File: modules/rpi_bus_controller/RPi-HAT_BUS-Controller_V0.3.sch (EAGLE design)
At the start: 66 parts, among them IC1 MC34063AD, IC2 ADUM1201ARZ, IC3 P89LPC922FDH,512FDH, IC4 24LC-I/OT, IC5 LPC1115, Q1 ASF1, T1 BC856, T2 BCP52, T3 BC847

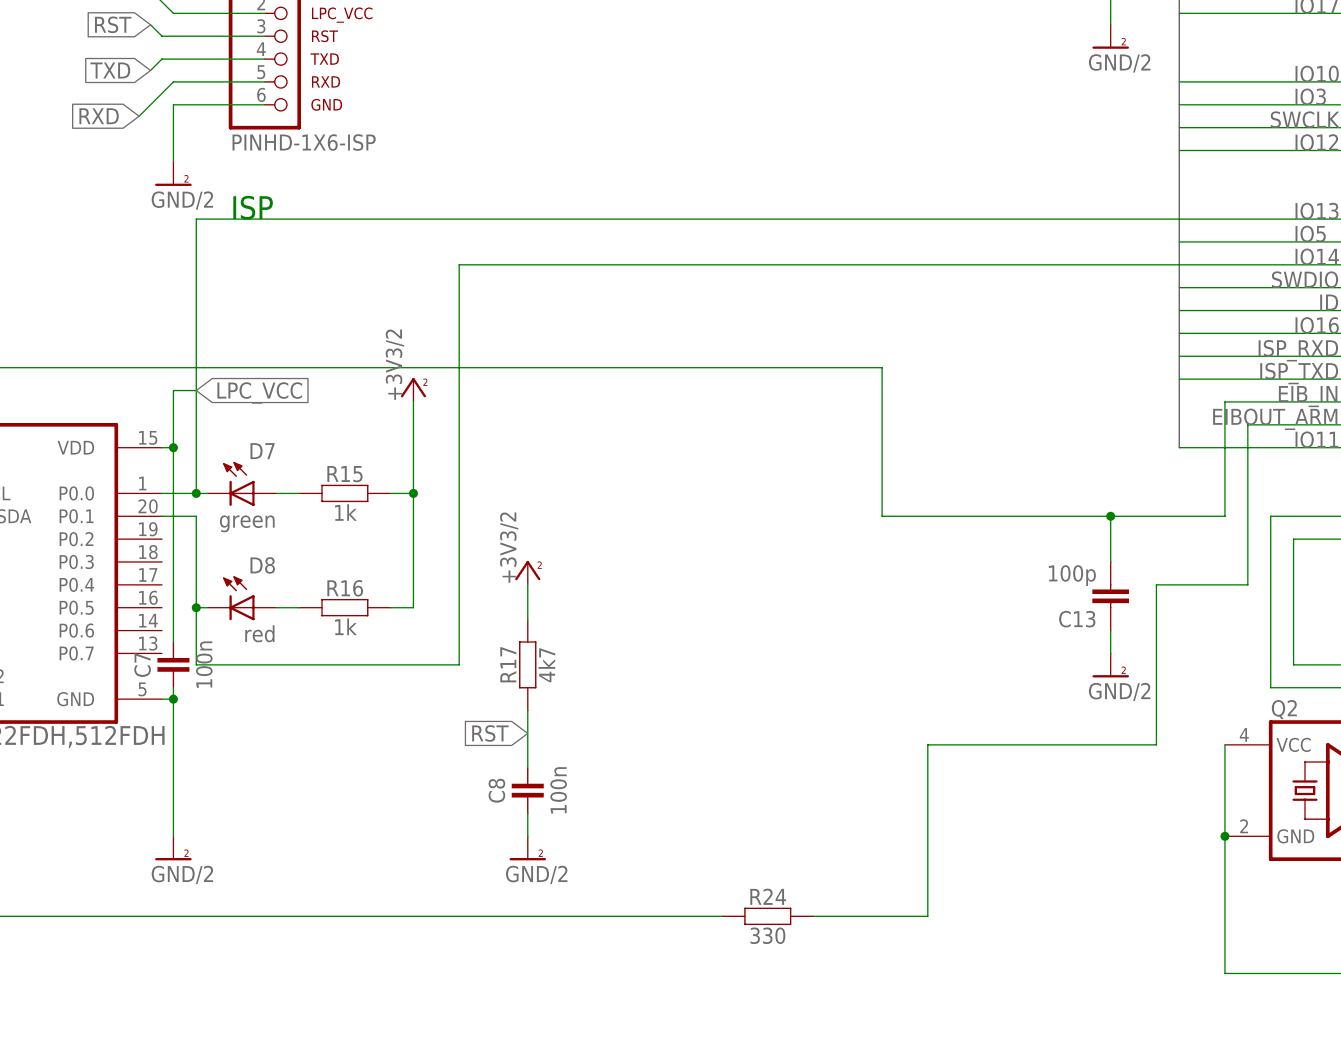
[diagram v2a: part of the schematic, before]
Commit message: schaltregler modifiziert, LEDs für ARM eingefügt und enable R für 922
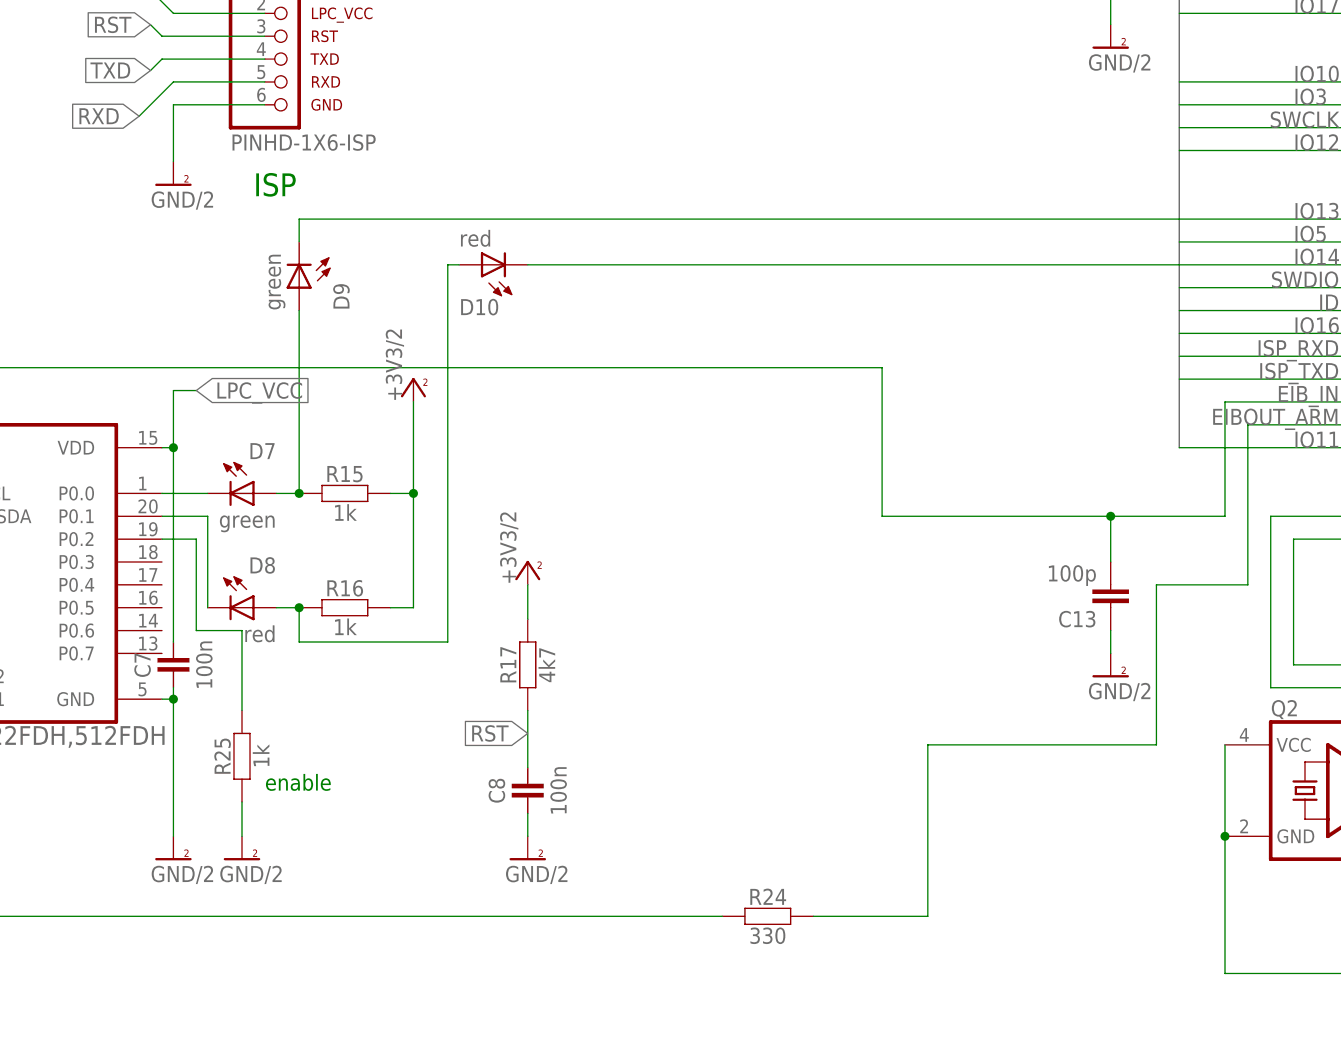
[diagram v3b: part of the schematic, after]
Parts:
- added D10: red, Diode_for_Selfbus-Projects:LED1206
- added D9: green, Diode_for_Selfbus-Projects:LED1206
- added R25: 1k, RCL_for_Selfbus-Projects:RESISTORR1206
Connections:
- new net N$11: D7.C, IC3.P0.0
- new net N$14: IC3.P0.2, R25.2
- new net N$9: D8.C, IC3.P0.1
- net GND/2: now also R25.1
- net IO12: now also D10.C; no longer D8.C, IC3.P0.1
- net IO15: now also D9.C; no longer D7.C, IC3.P0.0
- net N$35: now also D9.A
- net N$38: now also D10.A
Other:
- note added: "enable"
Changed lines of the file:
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@@
 <part name="R23" library="RCL_for_Selfbus-Projects" deviceset="RESISTOR" device="R1206" value="330"/>
 <part name="R24" library="RCL_for_Selfbus-Projects" deviceset="RESISTOR" device="R1206" value="330"/>
+<part name="D9" library="Diode_for_Selfbus-Projects" deviceset="LED" device="1206" value="green"/>
+<part name="D10" library="Diode_for_Selfbus-Projects" deviceset="LED" device="1206" value="red"/>
+<part name="R25" library="RCL_for_Selfbus-Projects" deviceset="RESISTOR" device="R1206" value="1k"/>
+<part name="GNDI6" library="Supply_for_Selfbus-Projects" deviceset="GND/2" device=""/>
 </parts>
 <sheets>
@@
 <text x="127" y="1.27" size="2.54" layer="91" font="vector">KNX Send Circuit</text>
 <text x="129.54" y="88.9" size="2.54" layer="91" font="vector">Raspberry Pi B+, 2</text>
-<text x="311.15" y="88.9" size="2.54" layer="91" font="vector">ISP</text>
+<text x="313.69" y="91.44" size="2.54" layer="91" font="vector">ISP</text>
 <text x="243.84" y="0" size="2.54" layer="91" font="vector">LPC Circuit</text>
 <text x="210.82" y="88.9" size="2.54" layer="91" font="vector">ID EEPROM Device Tree</text>
+<text x="314.96" y="25.4" size="1.778" layer="91">enable</text>
 </plain>
 <instances>
@@
 <instance part="R23" gate="G$1" x="553.72" y="88.9"/>
 <instance part="R24" gate="G$1" x="370.84" y="11.43"/>
+<instance part="D9" gate="G$1" x="318.77" y="82.55" rot="MR90"/>
+<instance part="D10" gate="G$1" x="340.36" y="83.82" rot="MR180"/>
+<instance part="R25" gate="G$1" x="312.42" y="29.21" rot="R90"/>
+<instance part="GNDI6" gate="G$1" x="312.42" y="17.78"/>
 </instances>
 <busses>
@@
 <pinref part="R15" gate="G$1" pin="1"/>
 <wire x1="316.23" y1="58.42" x2="318.77" y2="58.42" width="0.1524" layer="91"/>
+<pinref part="D9" gate="G$1" pin="A"/>
+<wire x1="318.77" y1="78.74" x2="318.77" y2="58.42" width="0.1524" layer="91"/>
+<junction x="318.77" y="58.42"/>
 </segment>
 </net>
@@
 <pinref part="R16" gate="G$1" pin="1"/>
 <wire x1="316.23" y1="45.72" x2="318.77" y2="45.72" width="0.1524" layer="91"/>
+<pinref part="D10" gate="G$1" pin="A"/>
+<wire x1="336.55" y1="83.82" x2="335.28" y2="83.82" width="0.1524" layer="91"/>
+<wire x1="335.28" y1="83.82" x2="335.28" y2="41.91" width="0.1524" layer="91"/>
+<wire x1="335.28" y1="41.91" x2="318.77" y2="41.91" width="0.1524" layer="91"/>
+<wire x1="318.77" y1="41.91" x2="318.77" y2="45.72" width="0.1524" layer="91"/>
+<junction x="318.77" y="45.72"/>
 </segment>
 </net>
@@
 <wire x1="408.94" y1="110.49" x2="408.94" y2="114.3" width="0.1524" layer="91"/>
 </segment>
+<segment>
+<pinref part="GNDI6" gate="G$1" pin="GND/2"/>
+<pinref part="R25" gate="G$1" pin="1"/>
+<wire x1="312.42" y1="20.32" x2="312.42" y2="24.13" width="0.1524" layer="91"/>
+</segment>
 </net>
 <net name="EIB_IN" class="0">
@@
 </segment>
 <segment>
-<wire x1="416.56" y1="83.82" x2="336.55" y2="83.82" width="0.1524" layer="91"/>
-<wire x1="336.55" y1="83.82" x2="336.55" y2="39.37" width="0.1524" layer="91"/>
-<pinref part="D8" gate="G$1" pin="C"/>
-<wire x1="307.34" y1="55.88" x2="307.34" y2="45.72" width="0.1524" layer="91"/>
-<wire x1="307.34" y1="45.72" x2="308.61" y2="45.72" width="0.1524" layer="91"/>
-<pinref part="IC3" gate="A" pin="P0.1"/>
-<wire x1="307.34" y1="55.88" x2="303.53" y2="55.88" width="0.1524" layer="91"/>
-<wire x1="336.55" y1="39.37" x2="307.34" y2="39.37" width="0.1524" layer="91"/>
-<wire x1="307.34" y1="39.37" x2="307.34" y2="45.72" width="0.1524" layer="91"/>
-<junction x="307.34" y="45.72"/>
+<wire x1="416.56" y1="83.82" x2="344.17" y2="83.82" width="0.1524" layer="91"/>
+<pinref part="D10" gate="G$1" pin="C"/>
 </segment>
 </net>
@@
 </segment>
 <segment>
-<pinref part="D7" gate="G$1" pin="C"/>
-<pinref part="IC3" gate="A" pin="P0.0"/>
-<wire x1="308.61" y1="58.42" x2="307.34" y2="58.42" width="0.1524" layer="91"/>
-<wire x1="307.34" y1="58.42" x2="303.53" y2="58.42" width="0.1524" layer="91"/>
-<wire x1="416.56" y1="88.9" x2="307.34" y2="88.9" width="0.1524" layer="91"/>
-<wire x1="307.34" y1="88.9" x2="307.34" y2="58.42" width="0.1524" layer="91"/>
-<junction x="307.34" y="58.42"/>
+<wire x1="416.56" y1="88.9" x2="318.77" y2="88.9" width="0.1524" layer="91"/>
+<wire x1="318.77" y1="88.9" x2="318.77" y2="86.36" width="0.1524" layer="91"/>
+<pinref part="D9" gate="G$1" pin="C"/>
 </segment>
 </net>
@@
 </segment>
 </net>
+<net name="N$9" class="0">
+<segment>
+<pinref part="D8" gate="G$1" pin="C"/>
+<pinref part="IC3" gate="A" pin="P0.1"/>
+<wire x1="308.61" y1="55.88" x2="303.53" y2="55.88" width="0.1524" layer="91"/>
+<wire x1="308.61" y1="55.88" x2="308.61" y2="45.72" width="0.1524" layer="91"/>
+</segment>
+</net>
+<net name="N$11" class="0">
+<segment>
+<pinref part="IC3" gate="A" pin="P0.0"/>
+<pinref part="D7" gate="G$1" pin="C"/>
+<wire x1="308.61" y1="58.42" x2="303.53" y2="58.42" width="0.1524" layer="91"/>
+</segment>
+</net>
+<net name="N$14" class="0">
+<segment>
+<pinref part="IC3" gate="A" pin="P0.2"/>
+<wire x1="303.53" y1="53.34" x2="307.34" y2="53.34" width="0.1524" layer="91"/>
+<wire x1="307.34" y1="53.34" x2="307.34" y2="43.18" width="0.1524" layer="91"/>
+<pinref part="R25" gate="G$1" pin="2"/>
+<wire x1="307.34" y1="43.18" x2="312.42" y2="43.18" width="0.1524" layer="91"/>
+<wire x1="312.42" y1="43.18" x2="312.42" y2="34.29" width="0.1524" layer="91"/>
+</segment>
+</net>
